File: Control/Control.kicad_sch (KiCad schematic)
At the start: 98 parts

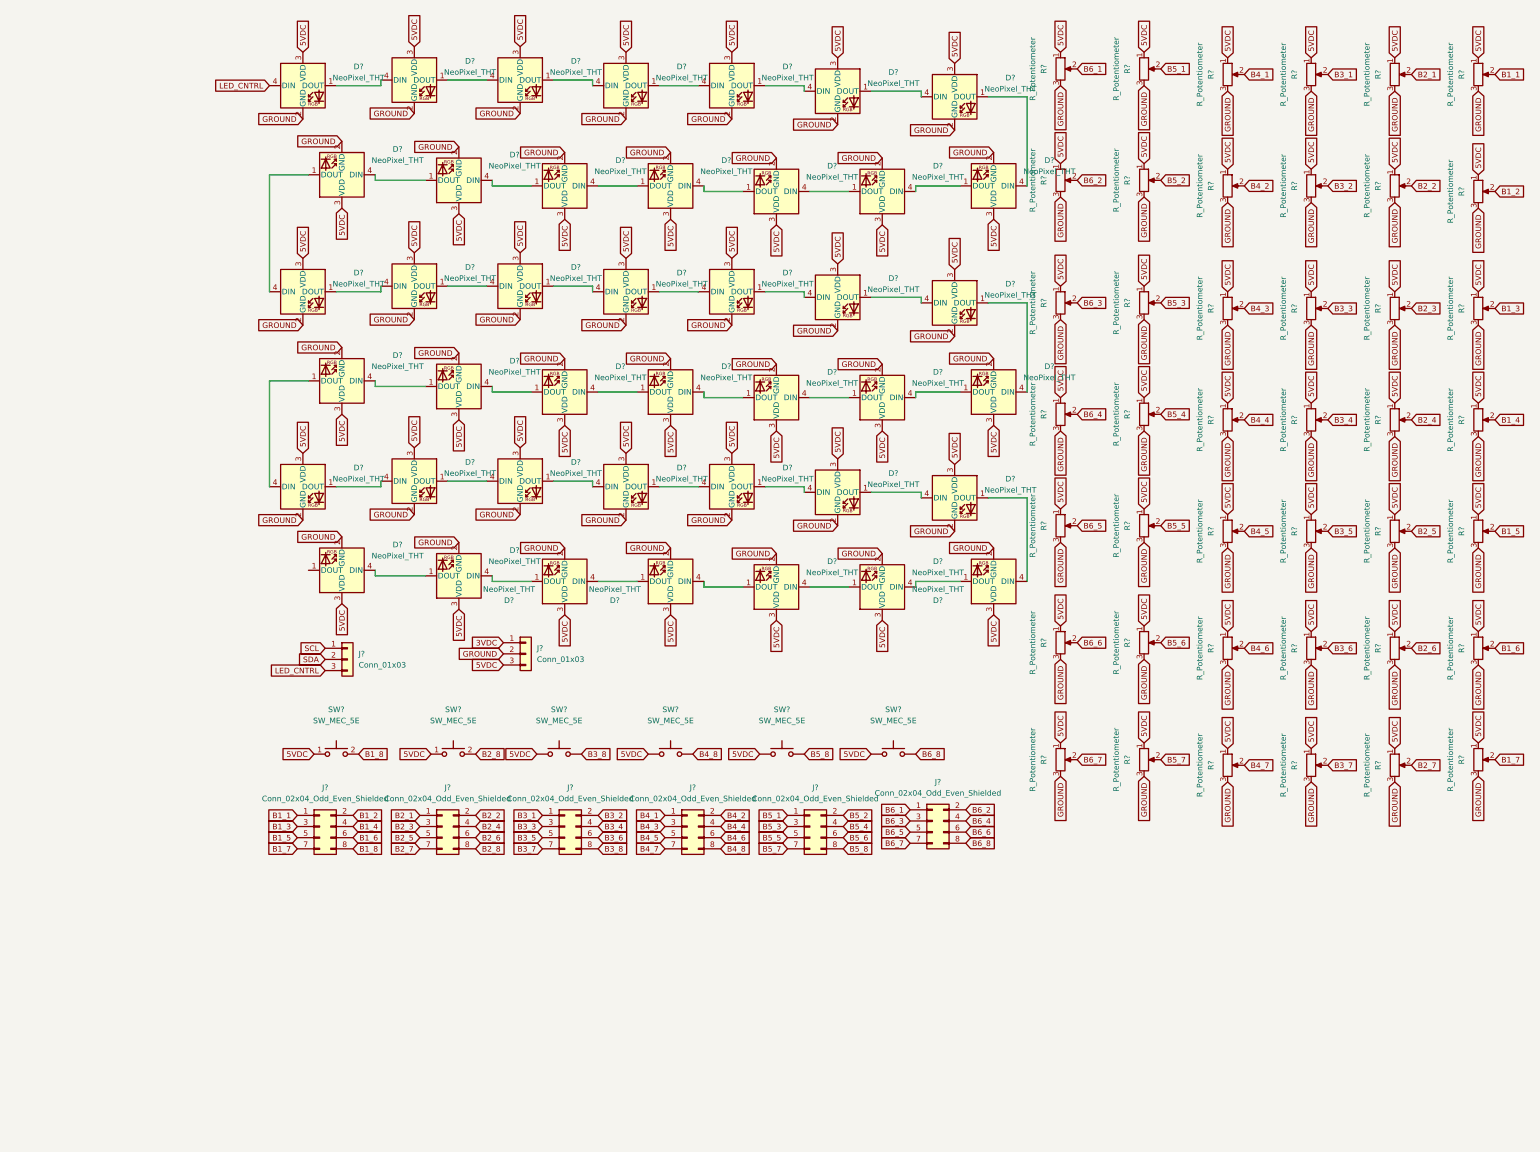
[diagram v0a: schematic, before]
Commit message: board config
will be resetting after finding a i2c oled on jlc
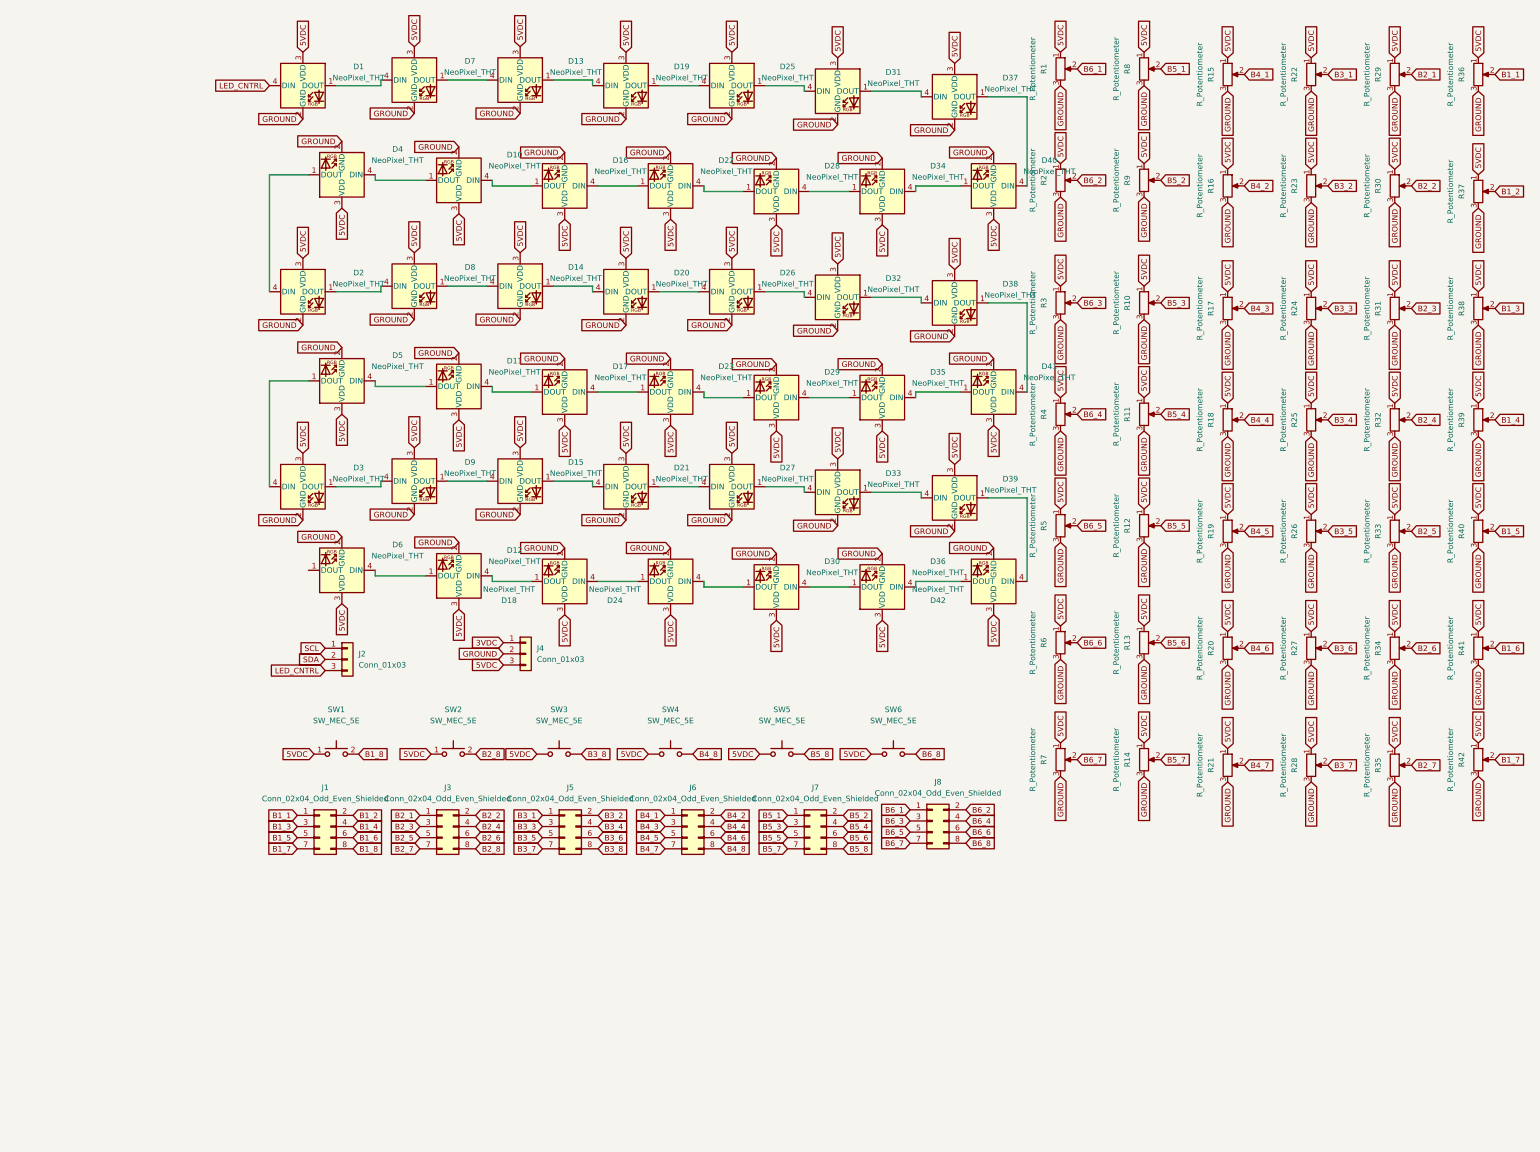
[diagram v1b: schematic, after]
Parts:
- J1, J3, J5, J6, J7, J8: renamed from J?; footprint Connector_PinHeader_1.00mm:PinHeader_2x08_P1.00mm_Vertical -> Connector_PinHeader_1.00mm:PinHeader_2x04_P1.00mm_Vertical
- gave numbers to parts that had none: 92

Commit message: cntrl gerber
easy eda routing
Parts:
- added C1, C4: 0.1uF cap, Capacitor_THT:C_Disc_D4.3mm_W1.9mm_P5.00mm, symbol pspice:CAP
- added C2: 4.7uF cap, Capacitor_THT:C_Disc_D4.3mm_W1.9mm_P5.00mm, symbol pspice:CAP
- added C3, C5: 4.7uF/16v, Capacitor_THT:C_Disc_D4.3mm_W1.9mm_P5.00mm, symbol pspice:CAP
- added DS1: OLED-128O064D, Display:OLED-128O064D, symbol Display_Graphic:OLED-128O064D
- added R43, R44: 2.2k, Resistor_THT:R_Box_L8.4mm_W2.5mm_P5.08mm, symbol Device:R
- added R45: 560k, Resistor_THT:R_Box_L8.4mm_W2.5mm_P5.08mm, symbol Device:R
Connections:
- net 3VDC: now also C1.1, C2.1, DS1.11 (BS1), DS1.9 (VDD)
- net 5VDC: now also C4.2, C5.2, DS1.28 (VCC)
- net GROUND: now also C1.2, C2.2, C3.2, C4.1, C5.1, DS1.1 (GND), DS1.10 (BS0), DS1.12 (BS2), DS1.13 (~{CS}), DS1.16 (R/~{W}), DS1.17 (E/~{RD}), DS1.21 (D3), DS1.22 (D4), DS1.23 (D5), DS1.24 (D6), DS1.25 (D7), DS1.29 (VLSS), DS1.30 (GND), DS1.8 (VSS), R43.1, R44.1, R45.2
- net SCL: now also DS1.18 (D0), R43.2
- net SDA: now also DS1.19 (D1), DS1.20 (D2), R44.2
- new net: DS1.26 (IREF), R45.1
- new net: C3.1, DS1.27 (VCOMH)
- no-connect marks 0 -> 4
